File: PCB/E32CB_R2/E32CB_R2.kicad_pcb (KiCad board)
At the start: 2 copper layers, 111.3 x 90.9 mm, 89 parts, among them J1 GPIO_HEADER, J10 S, J11 Q4, J12 S, J13 Q3, J14 S, J15 Q8, J16 S, J17 Q7, J18 S, J19 Q6, J2 Power, J20 S, J21 Q5, J22 S, J3 USB_B, J4 USB +5V, J5 NEXTION, J6 I2C, J7 Q1, J8 S, J9 Q2, Q1 S8050, Q10 IRLR2905, Q2 S8050, Q3 IRLR2905, Q4 IRLR2905, Q5 IRLR2905, Q6 IRLR2905, Q7 IRLR2905, Q8 IRLR2905, Q9 IRLR2905, U1 ESP32-WROOM-32, X1 12MHz

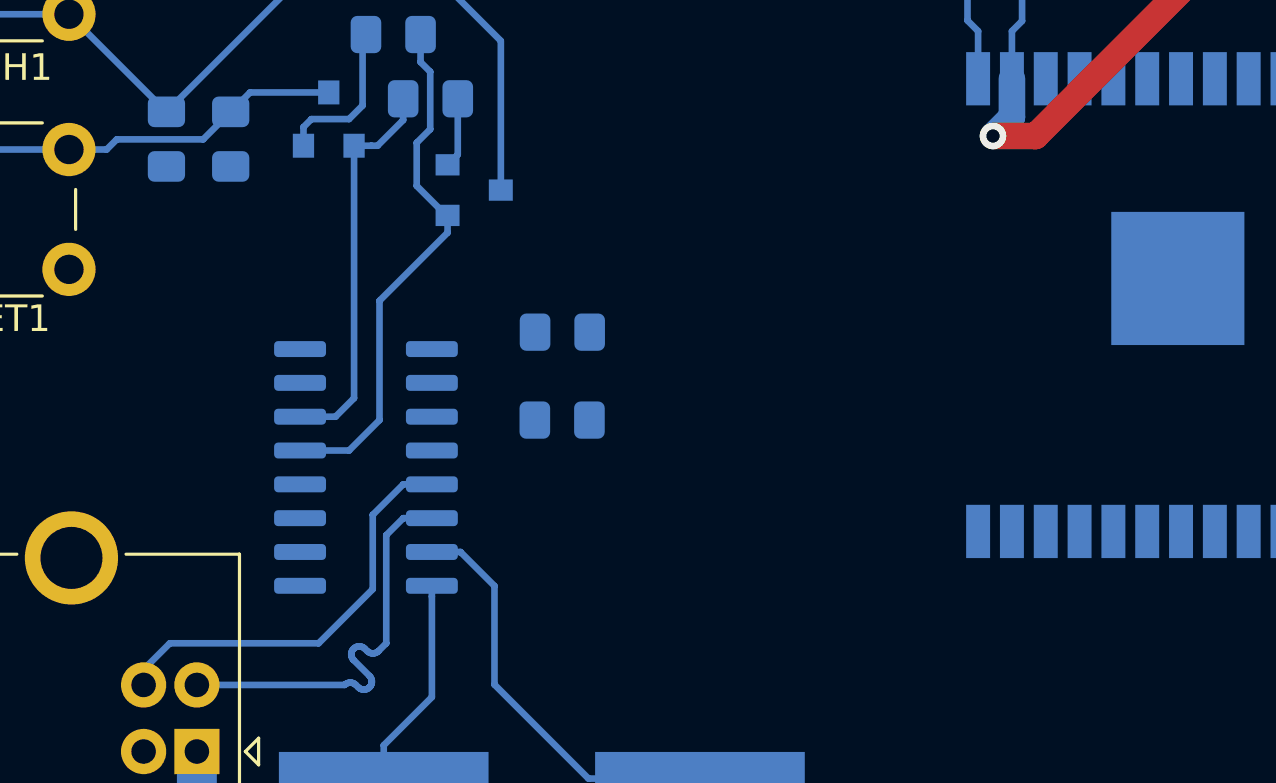
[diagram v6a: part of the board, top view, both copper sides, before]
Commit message: 3v3 update
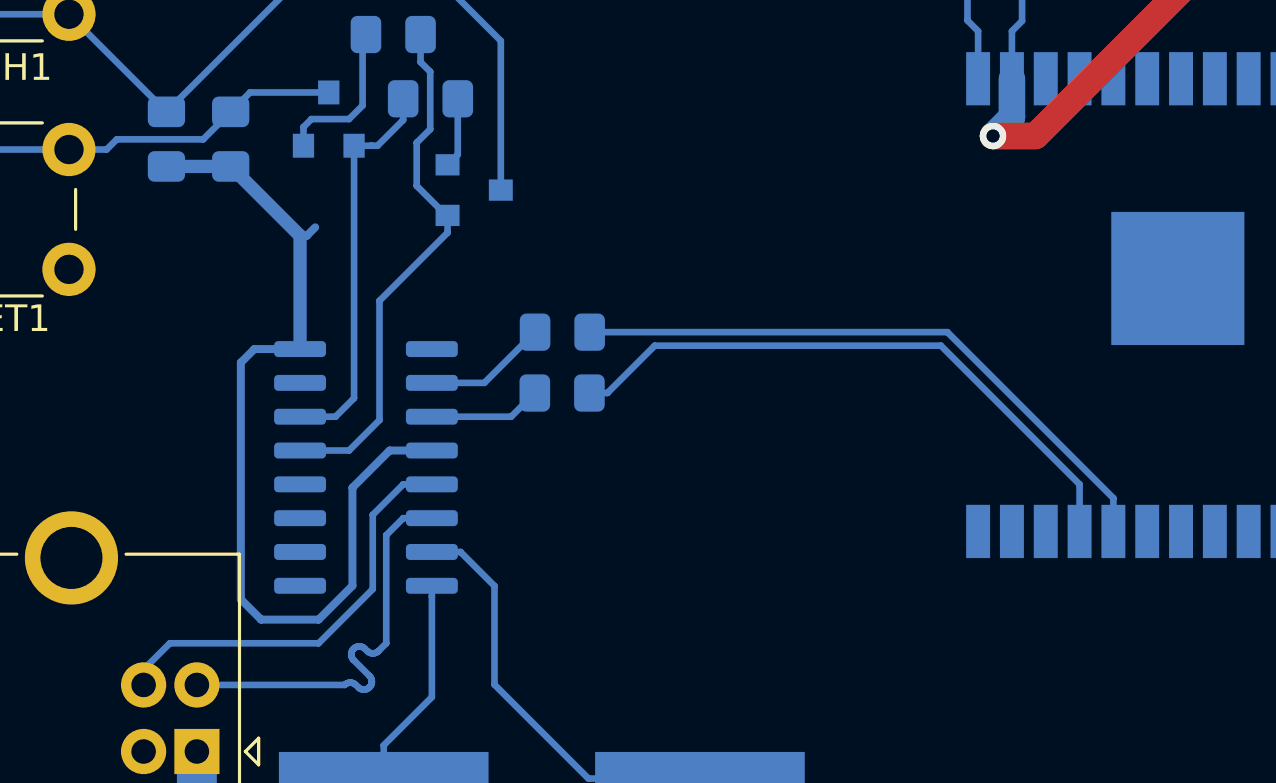
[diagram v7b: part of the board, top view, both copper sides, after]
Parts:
- moved R8 1.02 mm to (126.0, 79.0)
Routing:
- net +3V3: track 76.3 -> 111.0 mm
- net /RXD: track 0.00 -> 23.5 mm
- net /TXD: track 0.00 -> 23.1 mm
- net Net-(CH340G1-Pad2): track 0.00 -> 4.66 mm
- net Net-(CH340G1-Pad3): track 0.00 -> 4.23 mm
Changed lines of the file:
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@@
     (thickness 1.6)
     (drawings 8)
-    (tracks 455)
+    (tracks 481)
     (zones 0)
     (modules 89)
@@
   )
   (setup
-    (last_trace_width 1)
+    (last_trace_width 0.3)
     (user_trace_width 0.3)
     (user_trace_width 0.5)
@@
   )
   (module Resistor_SMD:R_0805_2012Metric_Pad1.15x1.40mm_HandSolder (layer B.Cu)
-    (at 125.984 80.01 180)
+    (at 125.984 78.994 180)
     (descr "Resistor SMD 0805 (2012 Metric), square (rectangular) end terminal, IPC_7351 nominal with elongated pad for handsoldering. (Body size source: https://docs.google.com/spreadsheets/d/1BsfQQcO9C6DZCsRaXUlFlo91Tg2WpOkGARC1WS5S8t0/edit?usp=sharing), generated with kicad-footprint-generator")
     (tags "resistor handsolder")
     (attr smd)
-    (fp_text reference R8 (at 0 1.65 180) (layer B.SilkS)
+    (fp_text reference R8 (at 0 -1.778 180) (layer B.SilkS)
       (effects (font (size 1 1) (thickness 0.15)) (justify mirror))
     )
@@
   (via (at 173.99 79.248) (size 1) (drill 0.5) (layers F.Cu B.Cu) (net 6))
   (segment (start 173.04 79.248) (end 172.348 78.556) (width 1) (layer B.Cu) (net 6))
-  (segment (start 143.256 63.5) (end 143.256 62.7) (width 0.25) (layer B.Cu) (net 6) (status 1000000))
-  (segment (start 143.256 62.7) (end 143.256 60.96) (width 0.25) (layer B.Cu) (net 6) (status 1000000))
-  (segment (start 143.256 65.024) (end 143.256 63.5) (width 0.25) (layer B.Cu) (net 6) (status 1000000))
-  (segment (start 142.875 65.405) (end 143.256 65.024) (width 0.25) (layer B.Cu) (net 6) (status 1000000))
-  (segment (start 142.875 67.192) (end 142.875 65.405) (width 0.25) (layer B.Cu) (net 6) (status 1000000))
-  (segment (start 142.875 68.632002) (end 142.165002 69.342) (width 1) (layer B.Cu) (net 6) (status 1000000))
-  (segment (start 142.875 67.192) (end 142.875 68.632002) (width 1) (layer B.Cu) (net 6) (status 1000000))
-  (segment (start 142.165002 69.342) (end 142.165002 69.342) (width 1) (layer B.Cu) (net 6) (status 1000000))
-  (via (at 142.165002 69.342) (size 1) (drill 0.5) (layers F.Cu B.Cu) (net 6))
+  (segment (start 143.256 63.5) (end 143.256 62.7) (width 0.25) (layer B.Cu) (net 6))
+  (segment (start 143.256 62.7) (end 143.256 60.96) (width 0.25) (layer B.Cu) (net 6))
+  (segment (start 143.256 65.024) (end 143.256 63.5) (width 0.25) (layer B.Cu) (net 6))
+  (segment (start 142.875 65.405) (end 143.256 65.024) (width 0.25) (layer B.Cu) (net 6))
+  (segment (start 142.875 67.192) (end 142.875 65.405) (width 0.25) (layer B.Cu) (net 6))
+  (segment (start 142.875 68.632002) (end 142.165002 69.342) (width 1) (layer B.Cu) (net 6))
+  (segment (start 142.875 67.192) (end 142.875 68.632002) (width 1) (layer B.Cu) (net 6))
+  (segment (start 142.165002 69.342) (end 142.165002 69.342) (width 1) (layer B.Cu) (net 6))
+  (via (at 142.165002 69.342) (size 1) (drill 0.5) (layers F.Cu B.Cu) (net 6) (status 1000000))
   (segment (start 173.99 79.248) (end 173.99 68.072) (width 1) (layer F.Cu) (net 6))
   (segment (start 173.99 68.072) (end 159.512 53.594) (width 1) (layer F.Cu) (net 6))
@@
   (segment (start 143.764 69.342) (end 159.512 53.594) (width 1) (layer F.Cu) (net 6))
   (segment (start 142.165002 69.342) (end 143.764 69.342) (width 1) (layer F.Cu) (net 6))
+  (segment (start 114.427 77.343) (end 116.143 77.343) (width 0.3) (layer B.Cu) (net 6))
+  (segment (start 119.507 81.153) (end 118.11 82.55) (width 0.3) (layer B.Cu) (net 6))
+  (segment (start 121.093 81.153) (end 119.507 81.153) (width 0.3) (layer B.Cu) (net 6))
+  (segment (start 113.919 77.851) (end 114.427 77.343) (width 0.3) (layer B.Cu) (net 6))
+  (segment (start 118.11 82.55) (end 118.11 86.233) (width 0.3) (layer B.Cu) (net 6))
+  (segment (start 113.919 86.741) (end 113.919 77.851) (width 0.3) (layer B.Cu) (net 6))
+  (segment (start 118.11 86.233) (end 116.84 87.503) (width 0.3) (layer B.Cu) (net 6))
+  (segment (start 116.84 87.503) (end 114.681 87.503) (width 0.3) (layer B.Cu) (net 6))
+  (segment (start 114.681 87.503) (end 113.919 86.741) (width 0.3) (layer B.Cu) (net 6))
+  (segment (start 116.143 73.09) (end 113.538 70.485) (width 0.5) (layer B.Cu) (net 6))
+  (segment (start 116.143 77.343) (end 116.143 73.09) (width 0.5) (layer B.Cu) (net 6))
+  (segment (start 113.538 70.485) (end 111.125 70.485) (width 0.5) (layer B.Cu) (net 6))
+  (segment (start 116.143 73.09) (end 116.394 73.09) (width 0.3) (layer B.Cu) (net 6))
+  (segment (start 116.394 73.09) (end 116.713 72.771) (width 0.3) (layer B.Cu) (net 6))
   (segment (start 187.836 78.74) (end 187.836 78.74) (width 3.7) (layer F.Cu) (net 7))
   (segment (start 202.24 78.74) (end 194.564 78.74) (width 3.7) (layer F.Cu) (net 7))
@@
   (segment (start 187.836 78.74) (end 187.08 77.984) (width 3.7) (layer F.Cu) (net 7))
   (via (at 187.96 79.756) (size 1) (drill 0.5) (layers F.Cu B.Cu) (net 7))
-  (segment (start 141.605 65.405) (end 141.206 65.006) (width 0.25) (layer B.Cu) (net 8) (status 1000000))
-  (segment (start 141.206 65.006) (end 141.206 63.5) (width 0.25) (layer B.Cu) (net 8) (status 1000000))
-  (segment (start 141.605 67.192) (end 141.605 65.405) (width 0.25) (layer B.Cu) (net 8) (status 1000000))
-  (segment (start 141.206 62.7) (end 141.206 60.96) (width 0.25) (layer B.Cu) (net 8) (status 1000000))
-  (segment (start 141.206 63.5) (end 141.206 62.7) (width 0.25) (layer B.Cu) (net 8) (status 1000000))
+  (segment (start 141.605 65.405) (end 141.206 65.006) (width 0.25) (layer B.Cu) (net 8))
+  (segment (start 141.206 65.006) (end 141.206 63.5) (width 0.25) (layer B.Cu) (net 8))
+  (segment (start 141.605 67.192) (end 141.605 65.405) (width 0.25) (layer B.Cu) (net 8))
+  (segment (start 141.206 62.7) (end 141.206 60.96) (width 0.25) (layer B.Cu) (net 8))
+  (segment (start 141.206 63.5) (end 141.206 62.7) (width 0.25) (layer B.Cu) (net 8))
   (segment (start 187.244 90.932) (end 187.244 90.932) (width 3.7) (layer F.Cu) (net 9))
   (segment (start 202.296 90.932) (end 194.564 90.932) (width 3.7) (layer F.Cu) (net 9))
@@
   (segment (start 118.491 65.659) (end 118.618 65.532) (width 0.25) (layer B.Cu) (net 37))
   (segment (start 116.271 69.007) (end 116.571 68.707) (width 0.25) (layer B.Cu) (net 37))
+  (segment (start 145.415 82.423) (end 145.415 84.192) (width 0.25) (layer B.Cu) (net 38))
+  (segment (start 129.462 77.216) (end 140.208 77.216) (width 0.25) (layer B.Cu) (net 38))
+  (segment (start 140.208 77.216) (end 145.415 82.423) (width 0.25) (layer B.Cu) (net 38))
+  (segment (start 127.009 78.994) (end 127.684 78.994) (width 0.25) (layer B.Cu) (net 38))
+  (segment (start 127.684 78.994) (end 129.462 77.216) (width 0.25) (layer B.Cu) (net 38))
+  (segment (start 124.07 79.883) (end 124.959 78.994) (width 0.25) (layer B.Cu) (net 39))
+  (segment (start 121.093 79.883) (end 124.07 79.883) (width 0.25) (layer B.Cu) (net 39))
+  (segment (start 123.063 78.613) (end 124.968 76.708) (width 0.25) (layer B.Cu) (net 40))
+  (segment (start 121.093 78.613) (end 123.063 78.613) (width 0.25) (layer B.Cu) (net 40))
+  (segment (start 146.685 82.942) (end 146.685 84.192) (width 0.25) (layer B.Cu) (net 41))
+  (segment (start 127.018 76.708) (end 140.451 76.708) (width 0.25) (layer B.Cu) (net 41))
+  (segment (start 140.451 76.708) (end 146.685 82.942) (width 0.25) (layer B.Cu) (net 41))
   (segment (start 119.126 115.872) (end 119.126 115.872) (width 3.7) (layer F.Cu) (net 43))
   (segment (start 119.126 130.8) (end 119.126 122.936) (width 3.7) (layer F.Cu) (net 43))

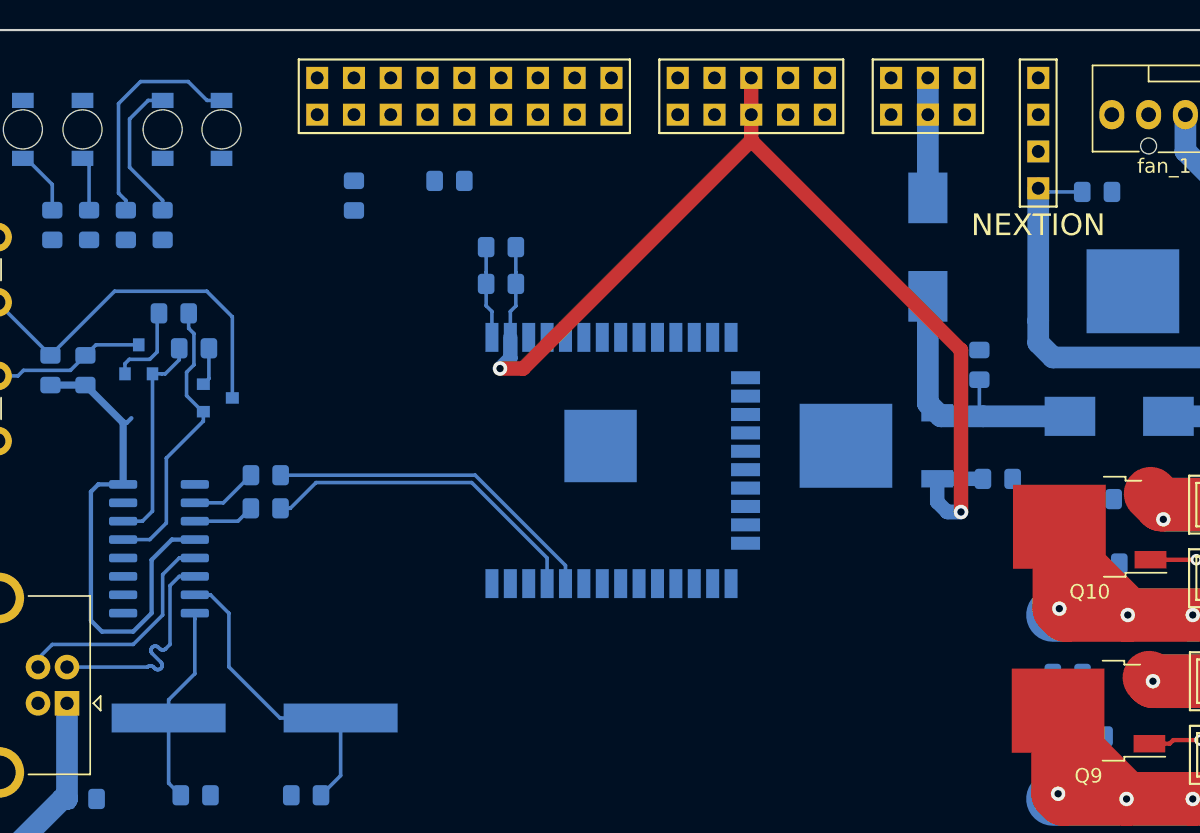
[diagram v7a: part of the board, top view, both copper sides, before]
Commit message: gpio neprohozeny
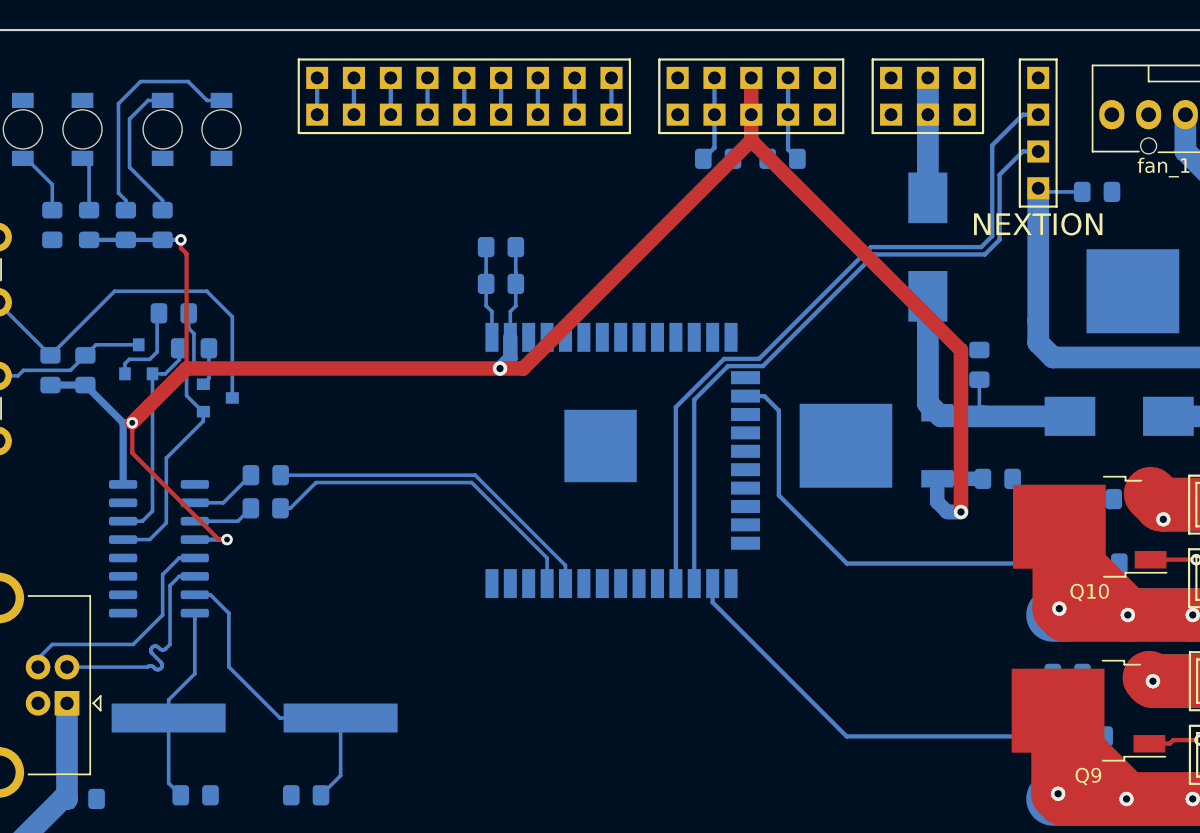
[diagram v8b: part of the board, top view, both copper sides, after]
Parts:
- moved R5 25.3 mm to (157.2, 54.9), turned to 180 degrees
- moved R6 23.0 mm to (161.7, 54.9)
- turned R23 to 180 degrees
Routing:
- net /U2_TXD: track 0.00 -> 49.2 mm
- net /U2_RXD: track 0.00 -> 46.2 mm
- net +3V3: track 111.0 -> 153.2 mm, vias 2 -> 5
- net /Q5: track 0.00 -> 32.0 mm
- net /Q6: track 0.00 -> 30.1 mm
- net /I2C_SDA: track 0.00 -> 5.91 mm
- net /I2C_SCL: track 0.00 -> 5.85 mm
- net /gpio5: track 0.00 -> 2.54 mm
- net /gpio26: track 0.00 -> 2.54 mm
- net /gpio2: track 0.00 -> 2.54 mm
- net /gpio15: track 0.00 -> 2.54 mm
- net /gpio12: track 0.00 -> 2.54 mm
- net /gpi39: track 0.00 -> 2.54 mm
- net /gpi36: track 0.00 -> 2.54 mm
- net /gpi35: track 0.00 -> 2.54 mm
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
